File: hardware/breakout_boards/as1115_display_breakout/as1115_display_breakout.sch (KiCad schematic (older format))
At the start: 5 parts, among them J1 7SEG_DEBUG, U1 AS1115, U2 LTC-4727JS

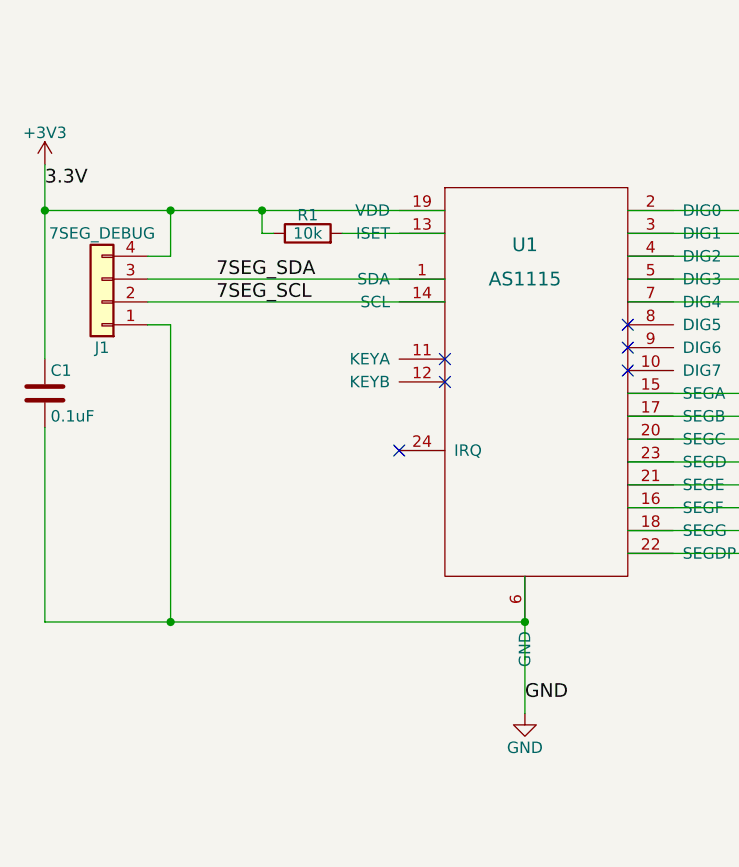
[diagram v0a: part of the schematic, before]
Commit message: Display breakout PCB layout
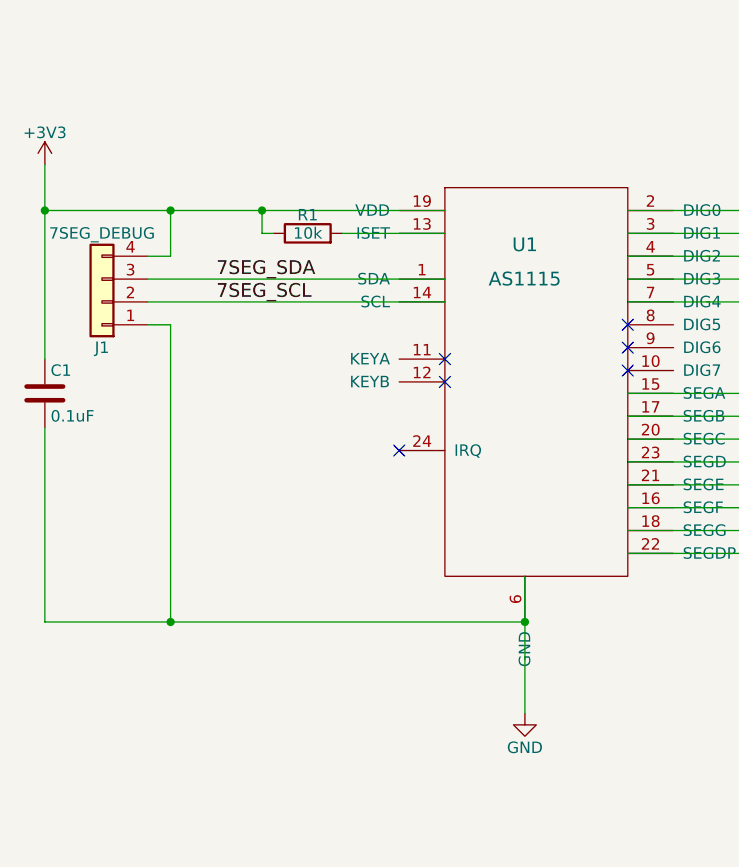
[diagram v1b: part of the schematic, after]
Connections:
- net labels removed: 3.3V
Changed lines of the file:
@@
 	1    0    0    -1
 $EndComp
-Text Label 4300 4600 0    60   ~ 0
-GND
 $Comp
 L device:R R1
@@
 NoConn ~ 4750 3050
 NoConn ~ 4750 3150
-Text Label 2200 2350 0    60   ~ 0
-3.3V
 Text Label 2950 2750 0    60   ~ 0
 7SEG_SDA

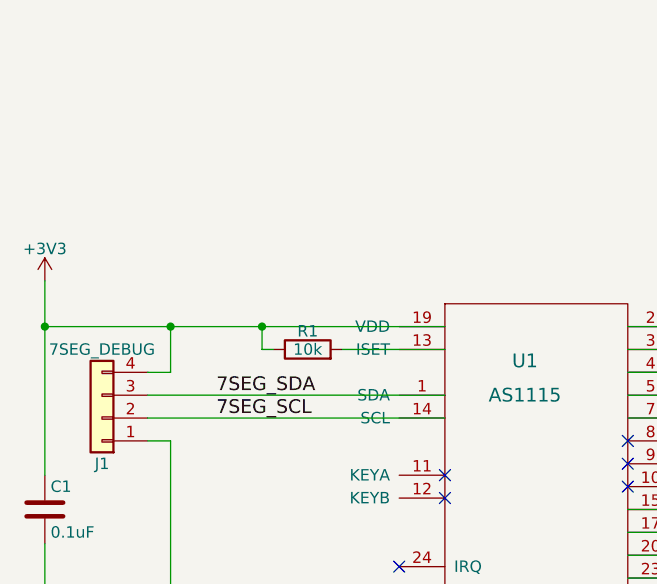
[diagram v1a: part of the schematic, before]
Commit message: Add pullup resistors, logo and text
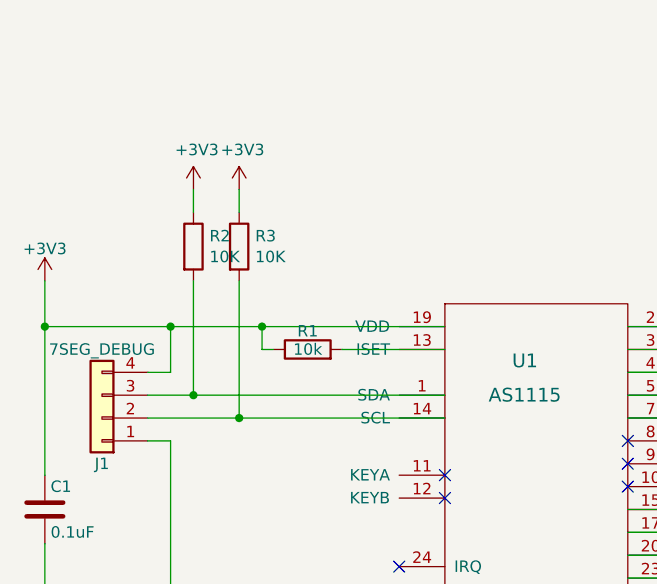
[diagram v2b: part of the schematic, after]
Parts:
- added R2, R3: 10K, symbol device:R
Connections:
- net labels removed: 7SEG_SCL, 7SEG_SDA
- wire segments 38 -> 42
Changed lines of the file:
@@
 NoConn ~ 4750 3050
 NoConn ~ 4750 3150
-Text Label 2950 2750 0    60   ~ 0
-7SEG_SDA
-Text Label 2950 2850 0    60   ~ 0
-7SEG_SCL
 Text Notes 10900 7650 0    60   ~ 12
 Status LED
@@
 Text Notes 14650 13150 0    60   ~ 0
 A
+Connection ~ 2850 2750
+$Comp
+L power:+3V3 #PWR?
+U 1 1 5A14990E
+P 2850 1850
+F 0 "#PWR?" H 2850 1700 50  0001 C CNN
+F 1 "+3V3" H 2865 2023 50  0000 C CNN
+F 2 "" H 2850 1850 50  0001 C CNN
+F 3 "" H 2850 1850 50  0001 C CNN
+	1    2850 1850
+	1    0    0    -1
+$EndComp
+$Comp
+L power:+3V3 #PWR?
+U 1 1 5A14993F
+P 3050 1850
+F 0 "#PWR?" H 3050 1700 50  0001 C CNN
+F 1 "+3V3" H 3065 2023 50  0000 C CNN
+F 2 "" H 3050 1850 50  0001 C CNN
+F 3 "" H 3050 1850 50  0001 C CNN
+	1    3050 1850
+	1    0    0    -1
+$EndComp
+$Comp
+L device:R R2
+U 1 1 5A14998C
+P 2850 2100
+F 0 "R2" H 2920 2146 50  0000 L CNN
+F 1 "10K" H 2920 2055 50  0000 L CNN
+F 2 "" V 2780 2100 50  0001 C CNN
+F 3 "" H 2850 2100 50  0001 C CNN
+	1    2850 2100
+	1    0    0    -1
+$EndComp
+$Comp
+L device:R R3
+U 1 1 5A149A1D
+P 3050 2100
+F 0 "R3" H 3120 2146 50  0000 L CNN
+F 1 "10K" H 3120 2055 50  0000 L CNN
+F 2 "" V 2980 2100 50  0001 C CNN
+F 3 "" H 3050 2100 50  0001 C CNN
+	1    3050 2100
+	1    0    0    -1
+$EndComp
+Wire Wire Line
+	2850 1850 2850 1950
+Wire Wire Line
+	2850 2250 2850 2750
+Wire Wire Line
+	3050 1850 3050 1950
+Wire Wire Line
+	3050 2250 3050 2850
+Connection ~ 3050 2850
 $EndSCHEMATC

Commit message: Add bill of materials for breakout boards
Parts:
- R2, R3: footprint (none) -> Resistors_SMD:R_0805_HandSoldering
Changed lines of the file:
@@
 Connection ~ 2850 2750
 $Comp
-L power:+3V3 #PWR?
+L power:+3V3 #PWR03
 U 1 1 5A14990E
 P 2850 1850
-F 0 "#PWR?" H 2850 1700 50  0001 C CNN
+F 0 "#PWR03" H 2850 1700 50  0001 C CNN
 F 1 "+3V3" H 2865 2023 50  0000 C CNN
 F 2 "" H 2850 1850 50  0001 C CNN
@@
 $EndComp
 $Comp
-L power:+3V3 #PWR?
+L power:+3V3 #PWR04
 U 1 1 5A14993F
 P 3050 1850
-F 0 "#PWR?" H 3050 1700 50  0001 C CNN
+F 0 "#PWR04" H 3050 1700 50  0001 C CNN
 F 1 "+3V3" H 3065 2023 50  0000 C CNN
 F 2 "" H 3050 1850 50  0001 C CNN
@@
 F 0 "R2" H 2920 2146 50  0000 L CNN
 F 1 "10K" H 2920 2055 50  0000 L CNN
-F 2 "" V 2780 2100 50  0001 C CNN
+F 2 "Resistors_SMD:R_0805_HandSoldering" V 2780 2100 50  0001 C CNN
 F 3 "" H 2850 2100 50  0001 C CNN
 	1    2850 2100
@@
 F 0 "R3" H 3120 2146 50  0000 L CNN
 F 1 "10K" H 3120 2055 50  0000 L CNN
-F 2 "" V 2980 2100 50  0001 C CNN
+F 2 "Resistors_SMD:R_0805_HandSoldering" V 2980 2100 50  0001 C CNN
 F 3 "" H 3050 2100 50  0001 C CNN
 	1    3050 2100
